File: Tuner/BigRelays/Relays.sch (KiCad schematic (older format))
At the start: 86 parts, among them J1 Conn_01x03, J10 Conn_01x02, J11 Conn_01x02, J12 Conn_01x01, J13 Conn_01x01, J14 Conn_01x01, J15 Conn_01x01, J16 Conn_01x02, J17 Conn_02x10_Odd_Even, J18 Conn_01x02, J19 Conn_01x03, J2 Conn_01x03, J3 Conn_01x03, J4 Conn_01x03, J5 Conn_01x03, J6 Conn_01x03, J7 Conn_01x03, J8 Conn_01x02, J9 Conn_01x02

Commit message: JLCPCB Nov 1 2018
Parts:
- removed C26: 10 nF, Capacitors_THT:C_Disc_D5.0mm_W2.5mm_P2.50mm, symbol C
- removed C27: 10 nF, Capacitors_THT:C_Disc_D5.0mm_W2.5mm_P5.00mm, symbol C
- added J21, J22, J23, J24, J25, J27, J28, J29, J30: Conn_01x01, tuner:SOLDERJUMPER, symbol Conn_01x01
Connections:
- net RFGND: now also J23.1 (Pin_1)
- net at J9.2 (Pin_2), RLY10.2 (NC): now also J24.1 (Pin_1)
- net at J10.2 (Pin_2), RLY10.3 (NO): now also J25.1 (Pin_1)
- net at J13.1 (Pin_1): now also J29.1 (Pin_1), J30.1 (Pin_1)
- net at J15.1 (Pin_1): now also J27.1 (Pin_1), J28.1 (Pin_1)
- net at J16.2 (Pin_2), RLY12.3 (NO): now also J21.1 (Pin_1)
- net at J11.2 (Pin_2), RLY12.2 (NC): now also J22.1 (Pin_1)
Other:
- moved on the sheet: J13, J15

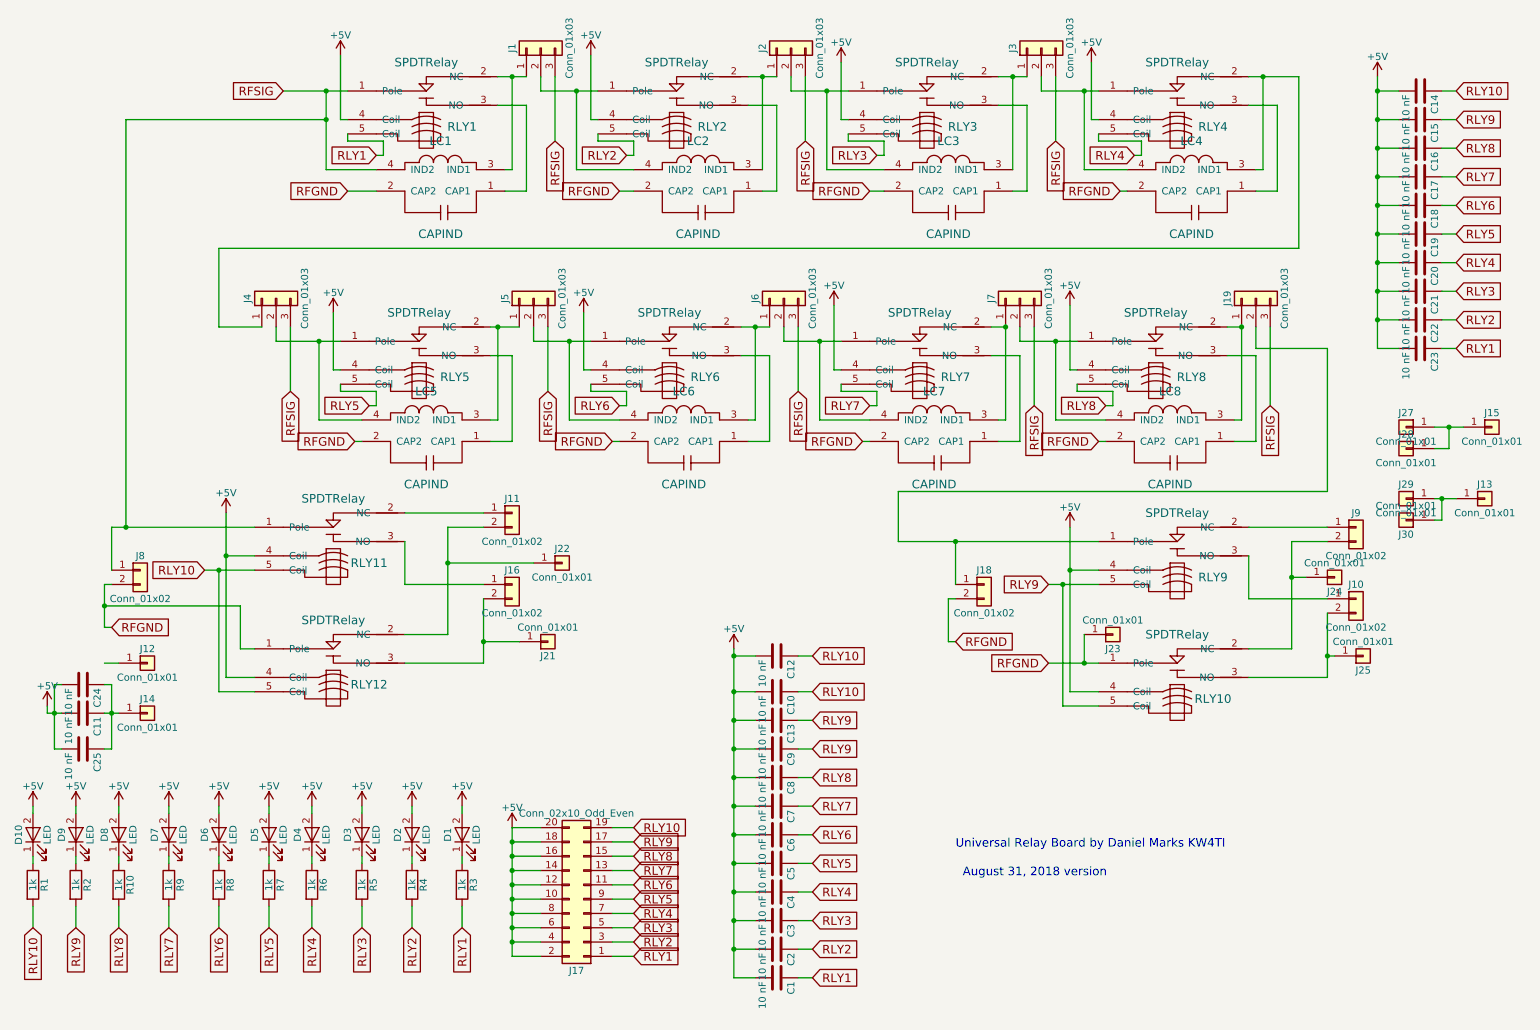
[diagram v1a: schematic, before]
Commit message: Added extra capacitors between relay power and ground posts
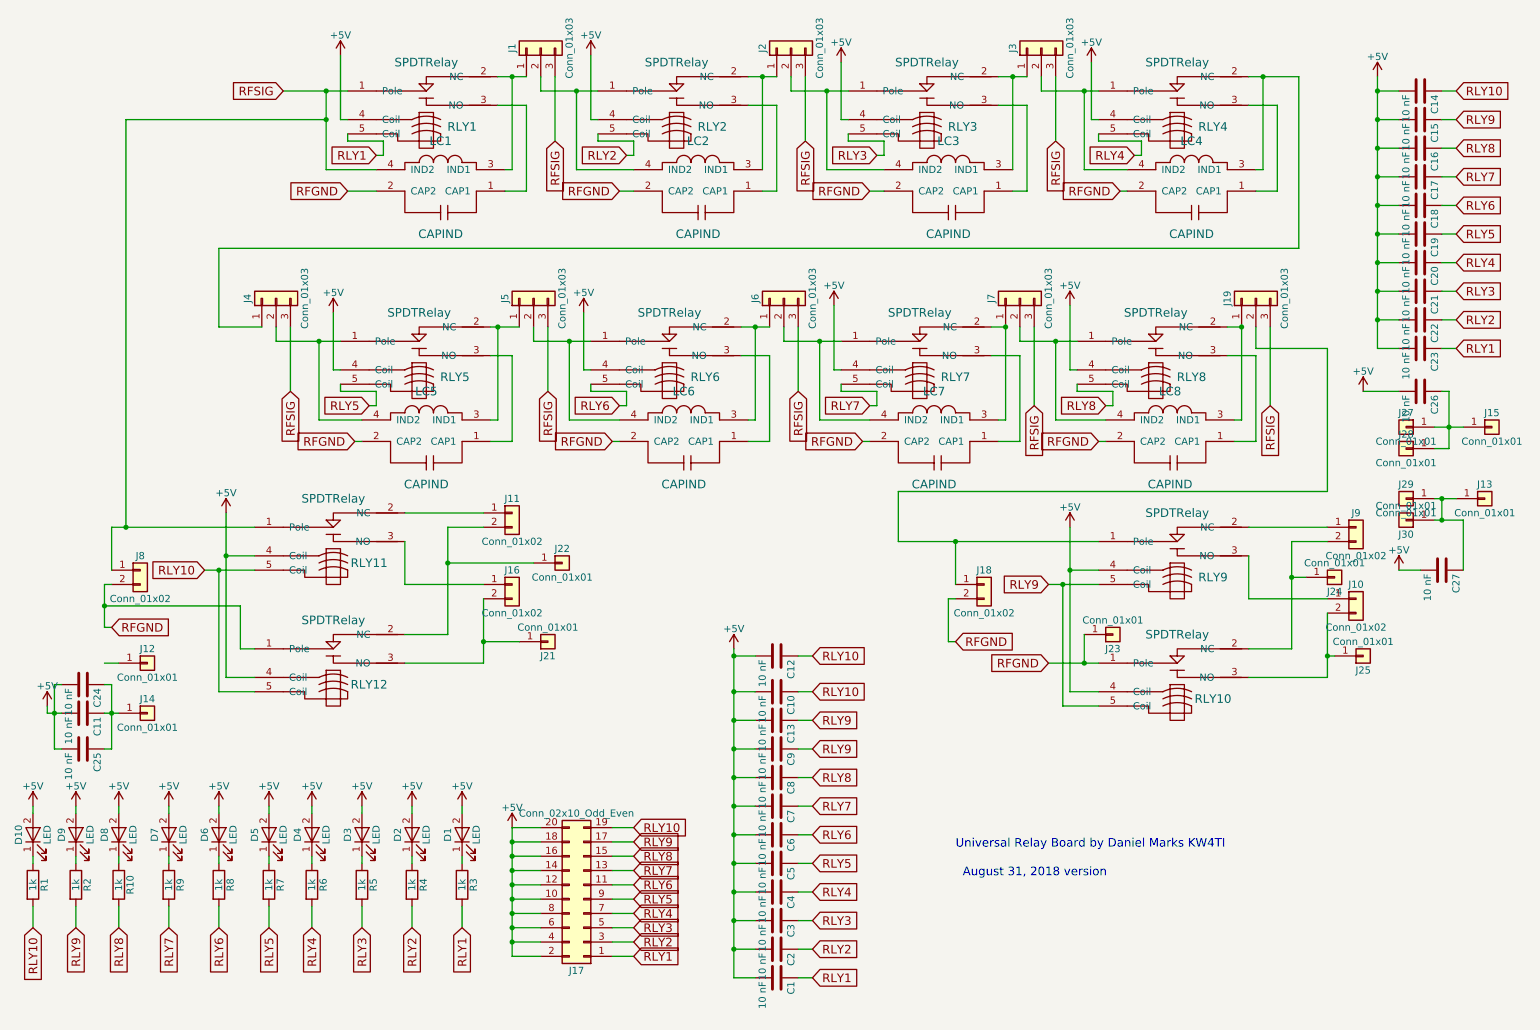
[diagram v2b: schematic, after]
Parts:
- added C26, C27: 10 nF, Capacitors_THT:C_Disc_D5.0mm_W2.5mm_P2.50mm, symbol C
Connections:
- net +5V: now also C26.2, C27.2
- net at J13.1 (Pin_1), J29.1 (Pin_1), J30.1 (Pin_1): now also C27.1
- net at J15.1 (Pin_1), J27.1 (Pin_1), J28.1 (Pin_1): now also C26.1
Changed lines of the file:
@@
 $EndComp
 $Comp
-L +5V #PWR01
+L +5V #PWR10
 U 1 1 5B1A3BAF
 P 2950 2950
-F 0 "#PWR01" H 2950 2800 50  0001 C CNN
+F 0 "#PWR10" H 2950 2800 50  0001 C CNN
 F 1 "+5V" H 2950 3090 50  0000 C CNN
 F 2 "" H 2950 2950 50  0001 C CNN
@@
 $EndComp
 $Comp
-L +5V #PWR02
+L +5V #PWR16
 U 1 1 5B1A3CC8
 P 4700 2950
-F 0 "#PWR02" H 4700 2800 50  0001 C CNN
+F 0 "#PWR16" H 4700 2800 50  0001 C CNN
 F 1 "+5V" H 4700 3090 50  0000 C CNN
 F 2 "" H 4700 2950 50  0001 C CNN
@@
 $EndComp
 $Comp
-L +5V #PWR03
+L +5V #PWR19
 U 1 1 5B1A3D42
 P 6450 2900
-F 0 "#PWR03" H 6450 2750 50  0001 C CNN
+F 0 "#PWR19" H 6450 2750 50  0001 C CNN
 F 1 "+5V" H 6450 3040 50  0000 C CNN
 F 2 "" H 6450 2900 50  0001 C CNN
@@
 $EndComp
 $Comp
-L +5V #PWR04
+L +5V #PWR22
 U 1 1 5B1A3DBC
 P 8100 4450
-F 0 "#PWR04" H 8100 4300 50  0001 C CNN
+F 0 "#PWR22" H 8100 4300 50  0001 C CNN
 F 1 "+5V" H 8100 4590 50  0000 C CNN
 F 2 "" H 8100 4450 50  0001 C CNN
@@
 $EndComp
 $Comp
-L +5V #PWR05
+L +5V #PWR23
 U 1 1 5B1A4C3F
 P 8250 1200
-F 0 "#PWR05" H 8250 1050 50  0001 C CNN
+F 0 "#PWR23" H 8250 1050 50  0001 C CNN
 F 1 "+5V" H 8250 1340 50  0000 C CNN
 F 2 "" H 8250 1200 50  0001 C CNN
@@
 $EndComp
 $Comp
-L +5V #PWR06
+L +5V #PWR20
 U 1 1 5B1A4CB9
 P 6500 1200
-F 0 "#PWR06" H 6500 1050 50  0001 C CNN
+F 0 "#PWR20" H 6500 1050 50  0001 C CNN
 F 1 "+5V" H 6500 1340 50  0000 C CNN
 F 2 "" H 6500 1200 50  0001 C CNN
@@
 $EndComp
 $Comp
-L +5V #PWR07
+L +5V #PWR17
 U 1 1 5B1A4D33
 P 4750 1150
-F 0 "#PWR07" H 4750 1000 50  0001 C CNN
+F 0 "#PWR17" H 4750 1000 50  0001 C CNN
 F 1 "+5V" H 4750 1290 50  0000 C CNN
 F 2 "" H 4750 1150 50  0001 C CNN
@@
 $EndComp
 $Comp
-L +5V #PWR08
+L +5V #PWR11
 U 1 1 5B1A4DAD
 P 3000 1150
-F 0 "#PWR08" H 3000 1000 50  0001 C CNN
+F 0 "#PWR11" H 3000 1000 50  0001 C CNN
 F 1 "+5V" H 3000 1290 50  0000 C CNN
 F 2 "" H 3000 1150 50  0001 C CNN
@@
 $EndComp
 $Comp
-L +5V #PWR09
+L +5V #PWR4
 U 1 1 5B25DE9C
 P 1450 6400
-F 0 "#PWR09" H 1450 6250 50  0001 C CNN
+F 0 "#PWR4" H 1450 6250 50  0001 C CNN
 F 1 "+5V" H 1450 6540 50  0000 C CNN
 F 2 "" H 1450 6400 50  0001 C CNN
@@
 $EndComp
 $Comp
-L +5V #PWR010
+L +5V #PWR5
 U 1 1 5B25F712
 P 1800 6400
-F 0 "#PWR010" H 1800 6250 50  0001 C CNN
+F 0 "#PWR5" H 1800 6250 50  0001 C CNN
 F 1 "+5V" H 1800 6540 50  0000 C CNN
 F 2 "" H 1800 6400 50  0001 C CNN
@@
 $EndComp
 $Comp
-L +5V #PWR011
+L +5V #PWR6
 U 1 1 5B25F91B
 P 2150 6400
-F 0 "#PWR011" H 2150 6250 50  0001 C CNN
+F 0 "#PWR6" H 2150 6250 50  0001 C CNN
 F 1 "+5V" H 2150 6540 50  0000 C CNN
 F 2 "" H 2150 6400 50  0001 C CNN
@@
 $EndComp
 $Comp
-L +5V #PWR012
+L +5V #PWR8
 U 1 1 5B25F931
 P 2500 6400
-F 0 "#PWR012" H 2500 6250 50  0001 C CNN
+F 0 "#PWR8" H 2500 6250 50  0001 C CNN
 F 1 "+5V" H 2500 6540 50  0000 C CNN
 F 2 "" H 2500 6400 50  0001 C CNN
@@
 $EndComp
 $Comp
-L +5V #PWR013
+L +5V #PWR9
 U 1 1 5B25FB4D
 P 2800 6400
-F 0 "#PWR013" H 2800 6250 50  0001 C CNN
+F 0 "#PWR9" H 2800 6250 50  0001 C CNN
 F 1 "+5V" H 2800 6540 50  0000 C CNN
 F 2 "" H 2800 6400 50  0001 C CNN
@@
 $EndComp
 $Comp
-L +5V #PWR014
+L +5V #PWR12
 U 1 1 5B25FB63
 P 3150 6400
-F 0 "#PWR014" H 3150 6250 50  0001 C CNN
+F 0 "#PWR12" H 3150 6250 50  0001 C CNN
 F 1 "+5V" H 3150 6540 50  0000 C CNN
 F 2 "" H 3150 6400 50  0001 C CNN
@@
 $EndComp
 $Comp
-L +5V #PWR015
+L +5V #PWR13
 U 1 1 5B25FB79
 P 3500 6400
-F 0 "#PWR015" H 3500 6250 50  0001 C CNN
+F 0 "#PWR13" H 3500 6250 50  0001 C CNN
 F 1 "+5V" H 3500 6540 50  0000 C CNN
 F 2 "" H 3500 6400 50  0001 C CNN
@@
 $EndComp
 $Comp
-L +5V #PWR016
+L +5V #PWR14
 U 1 1 5B25FB8F
 P 3850 6400
-F 0 "#PWR016" H 3850 6250 50  0001 C CNN
+F 0 "#PWR14" H 3850 6250 50  0001 C CNN
 F 1 "+5V" H 3850 6540 50  0000 C CNN
 F 2 "" H 3850 6400 50  0001 C CNN
@@
 RLY10
 $Comp
-L +5V #PWR017
+L +5V #PWR15
 U 1 1 5B89A678
 P 4200 6550
-F 0 "#PWR017" H 4200 6400 50  0001 C CNN
+F 0 "#PWR15" H 4200 6400 50  0001 C CNN
 F 1 "+5V" H 4200 6690 50  0000 C CNN
 F 2 "" H 4200 6550 50  0001 C CNN
@@
 $EndComp
 $Comp
-L +5V #PWR018
+L +5V #PWR3
 U 1 1 5B89BB19
 P 1150 6400
-F 0 "#PWR018" H 1150 6250 50  0001 C CNN
+F 0 "#PWR3" H 1150 6250 50  0001 C CNN
 F 1 "+5V" H 1150 6540 50  0000 C CNN
 F 2 "" H 1150 6400 50  0001 C CNN
@@
 $EndComp
 $Comp
-L +5V #PWR019
+L +5V #PWR1
 U 1 1 5B89BBCB
 P 850 6400
-F 0 "#PWR019" H 850 6250 50  0001 C CNN
+F 0 "#PWR1" H 850 6250 50  0001 C CNN
 F 1 "+5V" H 850 6540 50  0000 C CNN
 F 2 "" H 850 6400 50  0001 C CNN
@@
 RLY9
 $Comp
-L +5V #PWR020
+L +5V #PWR18
 U 1 1 5B89FB34
 P 5750 5300
-F 0 "#PWR020" H 5750 5150 50  0001 C CNN
+F 0 "#PWR18" H 5750 5150 50  0001 C CNN
 F 1 "+5V" H 5750 5440 50  0000 C CNN
 F 2 "" H 5750 5300 50  0001 C CNN
@@
 RLY8
 $Comp
-L +5V #PWR021
+L +5V #PWR21
 U 1 1 5B8A1B7B
 P 8100 2900
-F 0 "#PWR021" H 8100 2750 50  0001 C CNN
+F 0 "#PWR21" H 8100 2750 50  0001 C CNN
 F 1 "+5V" H 8100 3040 50  0000 C CNN
 F 2 "" H 8100 2900 50  0001 C CNN
@@
 $EndComp
 $Comp
-L +5V #PWR022
+L +5V #PWR7
 U 1 1 5B8A2542
 P 2200 4350
-F 0 "#PWR022" H 2200 4200 50  0001 C CNN
+F 0 "#PWR7" H 2200 4200 50  0001 C CNN
 F 1 "+5V" H 2200 4490 50  0000 C CNN
 F 2 "" H 2200 4350 50  0001 C CNN
@@
 $EndComp
 $Comp
-L +5V #PWR023
+L +5V #PWR2
 U 1 1 5B97C780
 P 950 5700
-F 0 "#PWR023" H 950 5550 50  0001 C CNN
+F 0 "#PWR2" H 950 5550 50  0001 C CNN
 F 1 "+5V" H 950 5840 50  0000 C CNN
 F 2 "" H 950 5700 50  0001 C CNN
@@
 RLY9
 $Comp
-L +5V #PWR024
+L +5V #PWR25
 U 1 1 5BA3849B
 P 10250 1300
-F 0 "#PWR024" H 10250 1150 50  0001 C CNN
+F 0 "#PWR25" H 10250 1150 50  0001 C CNN
 F 1 "+5V" H 10250 1440 50  0000 C CNN
 F 2 "" H 10250 1300 50  0001 C CNN
@@
 	10750 3900 10650 3900
 Wire Wire Line
-	10750 3750 10750 3900
+	10750 3500 10750 3900
 Connection ~ 10700 4250
 Wire Wire Line
 	10700 4400 10700 4250
 Wire Wire Line
-	10650 4400 10700 4400
+	10650 4400 10850 4400
 Connection ~ 3750 4700
 Wire Wire Line
@@
 	9700 1300 9700 2500
 Wire Wire Line
-	2150 2500 9700 2500
-Wire Wire Line
-	2150 3050 2150 2500
-Wire Wire Line
-	2450 3050 2150 3050
+	9700 2500 2150 2500
+Wire Wire Line
+	2150 2500 2150 3050
+Wire Wire Line
+	2150 3050 2450 3050
 Wire Wire Line
 	2650 3500 2650 3050
@@
 Wire Wire Line
 	2600 1400 3050 1400
+$Comp
+L +5V #PWR24
+U 1 1 5DDB7F4F
+P 10150 3500
+F 0 "#PWR24" H 10150 3350 50  0001 C CNN
+F 1 "+5V" H 10150 3640 50  0000 C CNN
+F 2 "" H 10150 3500 50  0001 C CNN
+F 3 "" H 10150 3500 50  0001 C CNN
+	1    10150 3500
+	1    0    0    -1
+$EndComp
+$Comp
+L C C26
+U 1 1 5DDB81E5
+P 10550 3500
+F 0 "C26" H 10575 3600 50  0000 L CNN
+F 1 "10 nF" H 10575 3400 50  0000 L CNN
+F 2 "Capacitors_THT:C_Disc_D5.0mm_W2.5mm_P2.50mm" H 10588 3350 50  0001 C CNN
+F 3 "" H 10550 3500 50  0001 C CNN
+	1    10550 3500
+	0    1    1    0
+$EndComp
+Wire Wire Line
+	10150 3500 10400 3500
+Wire Wire Line
+	10700 3500 10750 3500
+$Comp
+L +5V #PWR26
+U 1 1 5DDB884A
+P 10400 4750
+F 0 "#PWR26" H 10400 4600 50  0001 C CNN
+F 1 "+5V" H 10400 4890 50  0000 C CNN
+F 2 "" H 10400 4750 50  0001 C CNN
+F 3 "" H 10400 4750 50  0001 C CNN
+	1    10400 4750
+	1    0    0    -1
+$EndComp
+$Comp
+L C C27
+U 1 1 5DDB896F
+P 10700 4750
+F 0 "C27" H 10725 4850 50  0000 L CNN
+F 1 "10 nF" H 10725 4650 50  0000 L CNN
+F 2 "Capacitors_THT:C_Disc_D5.0mm_W2.5mm_P2.50mm" H 10738 4600 50  0001 C CNN
+F 3 "" H 10700 4750 50  0001 C CNN
+	1    10700 4750
+	0    1    1    0
+$EndComp
+Wire Wire Line
+	10550 4750 10400 4750
+Wire Wire Line
+	10850 4400 10850 4750
+Connection ~ 10700 4400
 $EndSCHEMATC
